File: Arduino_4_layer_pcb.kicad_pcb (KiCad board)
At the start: 2 copper layers, 41.4 x 27.9 mm, 17 parts, among them J1 Serial, J2 Digital pins, J3 ICSP connector, J4 I2C, U1 DS1337_AH, U2 24LC1025, U3 24LC1025, U4 ATMEGA328P-AU, Y1 Crystal 32MHZ, Y2 Crystal 16MHZ

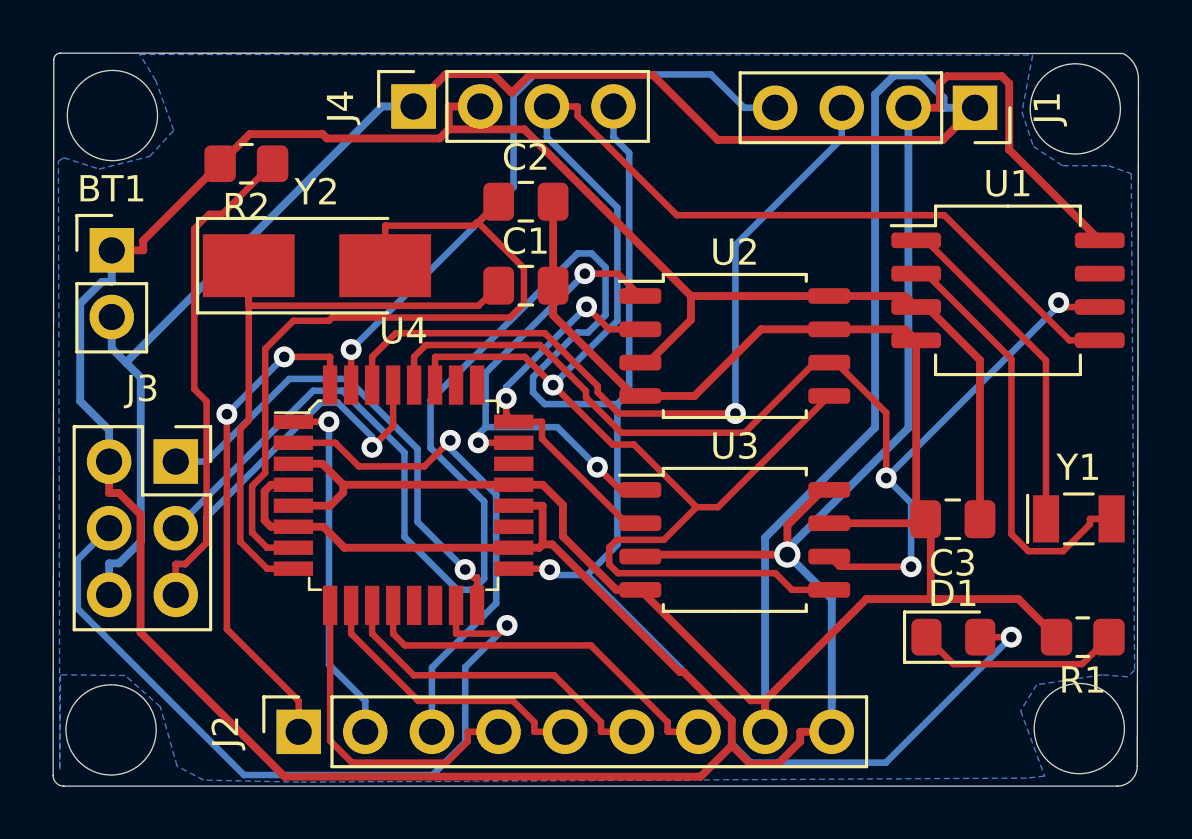
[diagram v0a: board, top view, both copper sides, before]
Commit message: Adding a filling layer to the 2 layer kicad_pcb
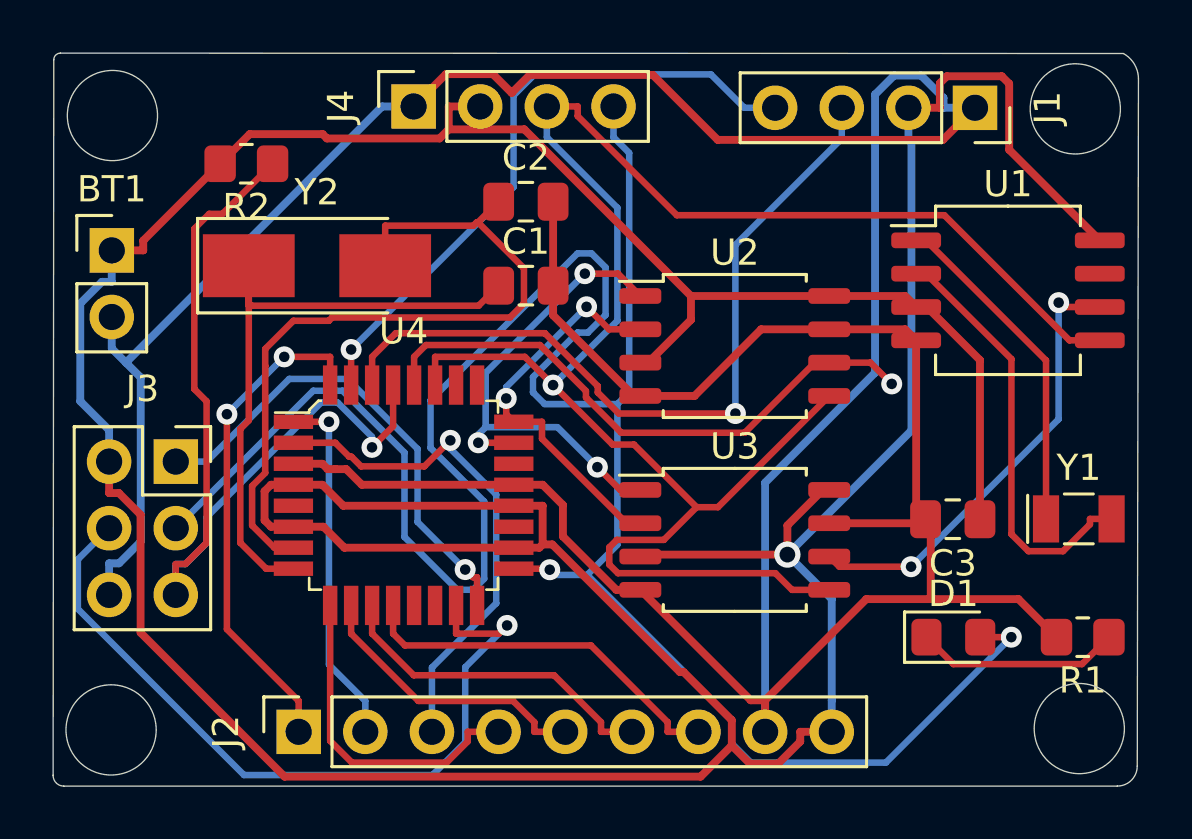
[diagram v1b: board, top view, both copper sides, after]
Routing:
- net /VCC: track 171.9 -> 180.7 mm
- net /SCL: track 43.3 -> 47.4 mm
- net GNDPWR: track 155.5 -> 153.1 mm
- removed copper zone on B.Cu, net GNDPWR
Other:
- copper layers 2 -> 4
